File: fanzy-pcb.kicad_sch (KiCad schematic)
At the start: 27 parts, among them J1 Conn_01x04_Pin, J2 Screw_Terminal_01x05, P1 USB_C_Plug_USB2.0, Q1 IRLZ44N, SW1 SW_Push, U1 STM32G030F6Px, U2 AMS1117-3.3, U3 CH340N, U4 YAAJ_DCDC_StepDown_LM2596

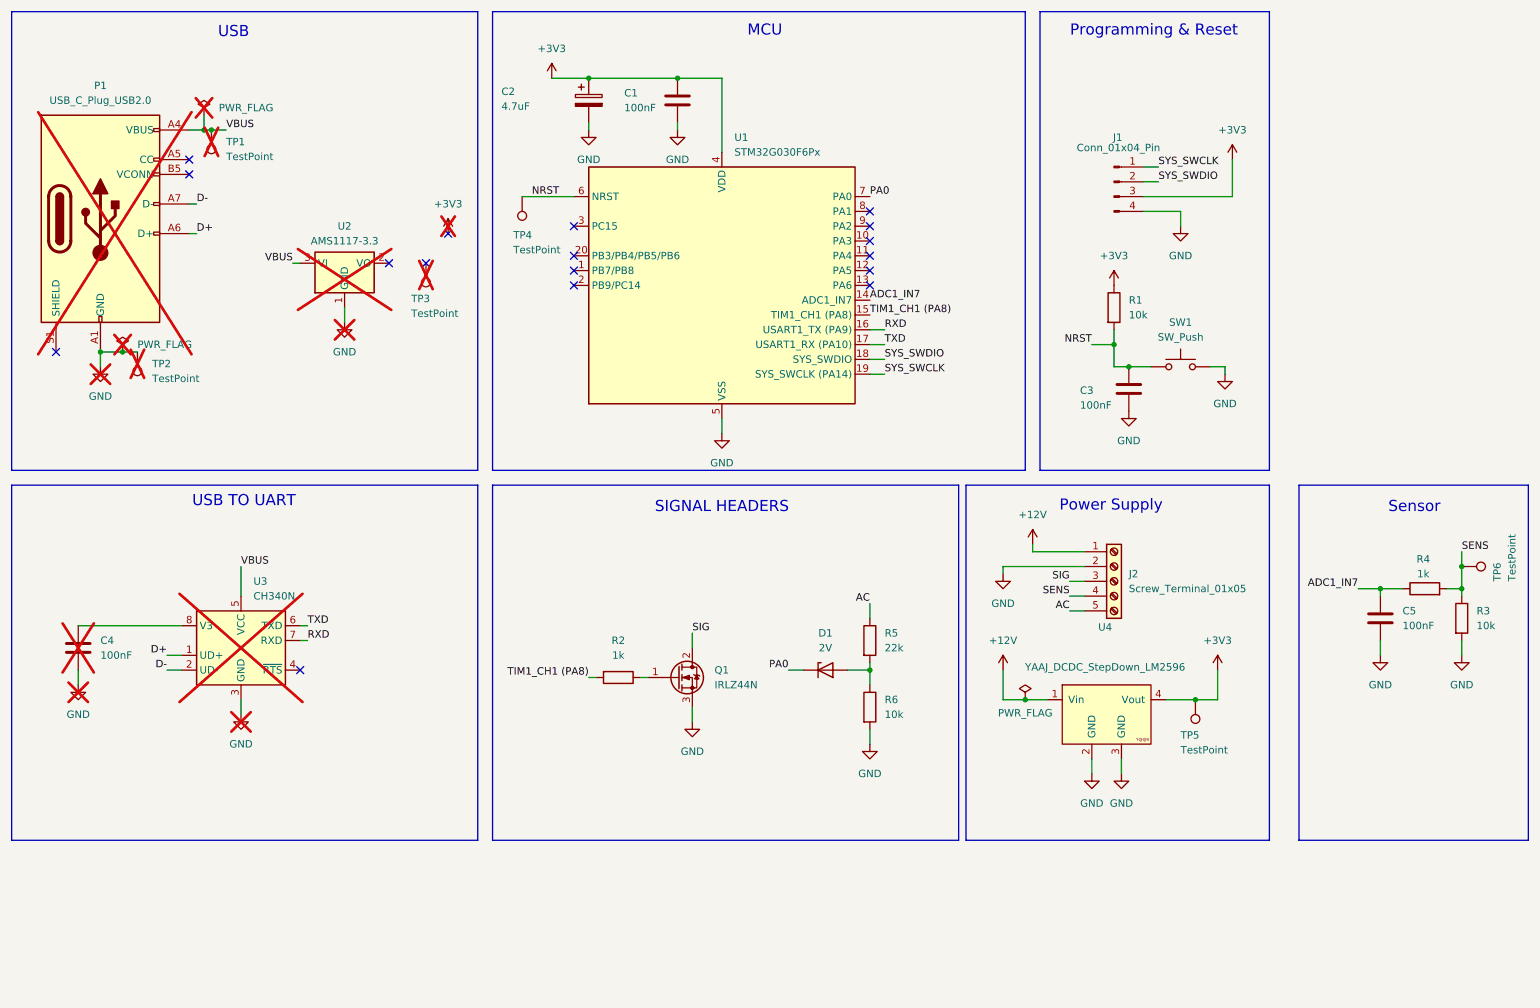
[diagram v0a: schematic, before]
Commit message: feat: uart port + rework
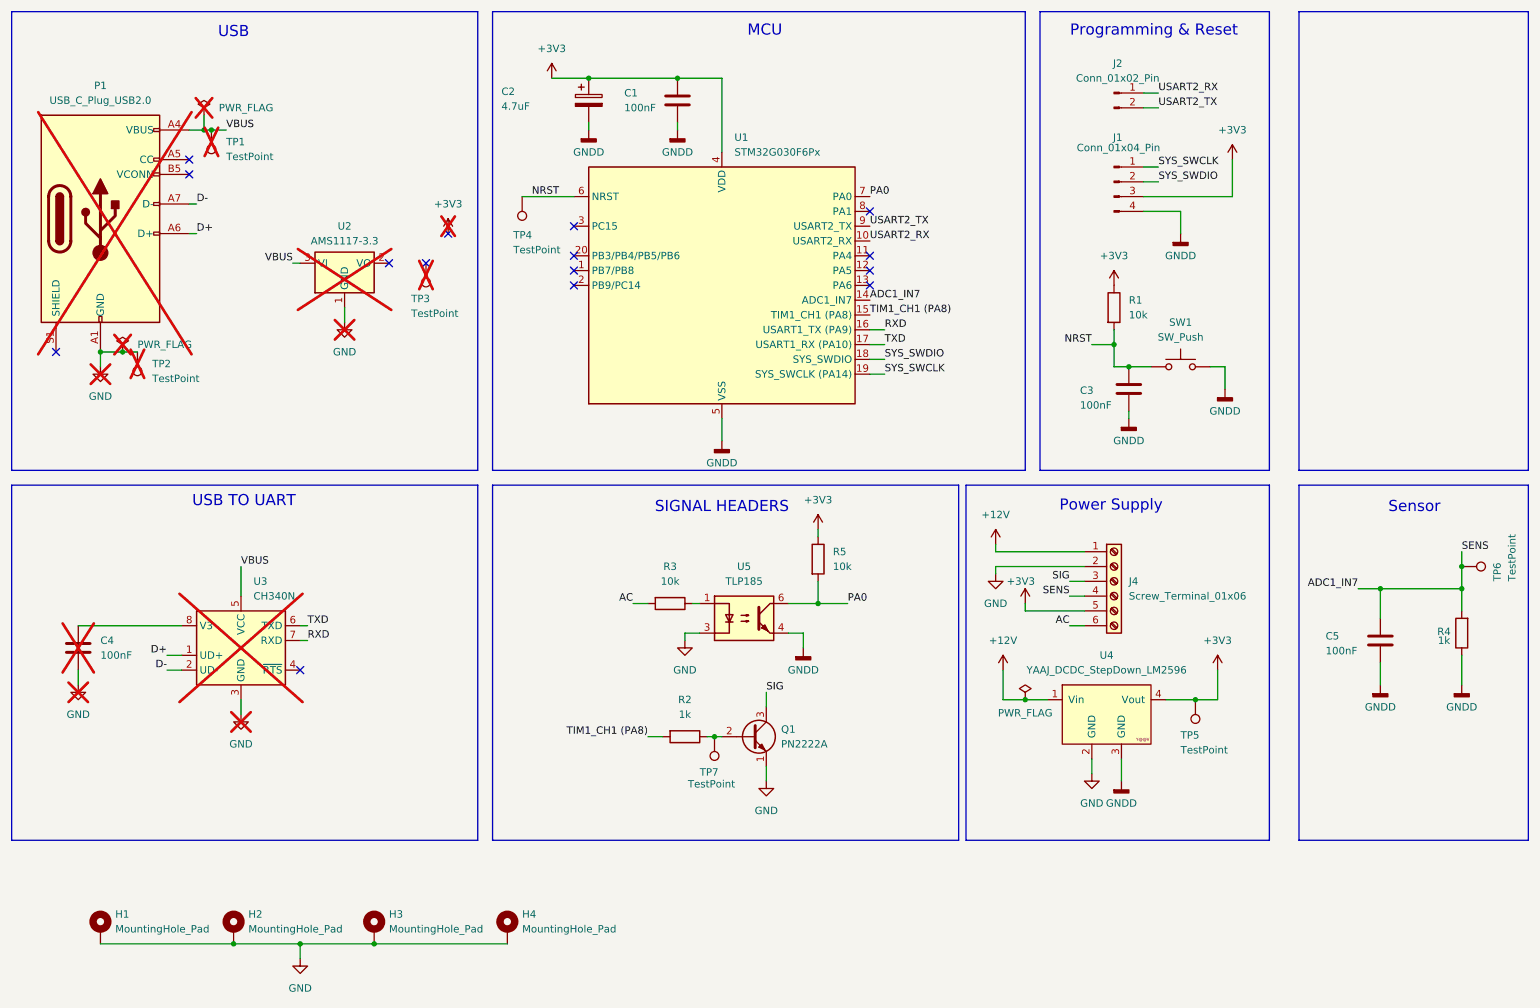
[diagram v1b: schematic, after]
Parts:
- removed D1: 2V, Diode_SMD:D_MiniMELF_Handsoldering, symbol Device:D_Zener
- removed J2: Screw_Terminal_01x05, TerminalBlock_Phoenix:TerminalBlock_Phoenix_MKDS-1,5-5-5.08_1x05_P5.08mm_Horizontal, symbol Connector:Screw_Terminal_01x05
- removed Q1: IRLZ44N, Package_TO_SOT_THT:TO-220-3_Vertical, symbol Transistor_FET:IRLZ44N
- removed R6: 10k, Resistor_SMD:R_0805_2012Metric_Pad1.20x1.40mm_HandSolder, symbol Device:R
- added H1, H2, H3, H4: MountingHole_Pad, MountingHole:MountingHole_3.2mm_M3_Pad_Via, symbol Mechanical:MountingHole_Pad
- added J2: Conn_01x02_Pin, Connector_PinHeader_2.54mm:PinHeader_1x02_P2.54mm_Vertical, symbol Connector:Conn_01x02_Pin
- added J4: Screw_Terminal_01x06, TerminalBlock_Phoenix:TerminalBlock_Phoenix_MKDS-1,5-6-5.08_1x06_P5.08mm_Horizontal, symbol Connector:Screw_Terminal_01x06
- added Q1: PN2222A, Package_TO_SOT_THT:TO-92_Inline, symbol Transistor_BJT:PN2222A
- added TP7: TestPoint, TestPoint:TestPoint_Pad_1.0x1.0mm, symbol Connector:TestPoint
- added U5: TLP185, Octocoupler:TLP185, symbol Isolator:TLP185
- R5: value 22k -> 10k
- SW1: footprint Button_Switch_SMD:SW_SPST_TL3342 -> Button_Switch_THT:SW_PUSH_6mm
- U4: footprint YAAJ:YAAJ_DCDC_StepDown_LM2596 -> DC-DC-Converters:YAAJ_DCDC_StepDown_LM2596
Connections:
- net +12V: now also J4.1 (Pin_1)
- net +3V3: now also R5.1, J4.5 (Pin_5)
- net AC: now also R3.2, J4.6 (Pin_6); no longer R5.1
- net ADC1_IN7: now also R4.2, TP6.1, J4.4 (Pin_4); no longer R4.1
- net GND: now also H1.1, H2.1, H3.1, H4.1, J4.2 (Pin_2), Q1.1 (E), U5.3; no longer C1.2, C2.2, C3.2, C5.2, J1.4 (Pin_4), R3.2, SW1.2, U1.5 (VSS), U4.3 (GND)
- net PA0: now also R5.2, U5.6
- net SIG: now also J4.3 (Pin_3), Q1.3 (C)
- net at R2.1: now also Q1.2 (B), TP7.1
- net USART2_RX: now reaches U1.10 (PA3)
- net USART2_RX: now also J2.1 (Pin_1)
- net USART2_TX: now reaches U1.9 (PA2)
- net USART2_TX: now also J2.2 (Pin_2)
- removed net SENS: R3.1, R4.2, TP6.1
- new net: R3.1, U5.1
- new net GNDD: C1.2, C2.2, C3.2, C5.2, J1.4 (Pin_4), R4.1, SW1.2, U1.5 (VSS), U4.3 (GND), U5.4
- no-connect marks 17 -> 15
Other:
- moved on the sheet: C5, R2, R4

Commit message: rework: switching to the STM32G031J6M6 series
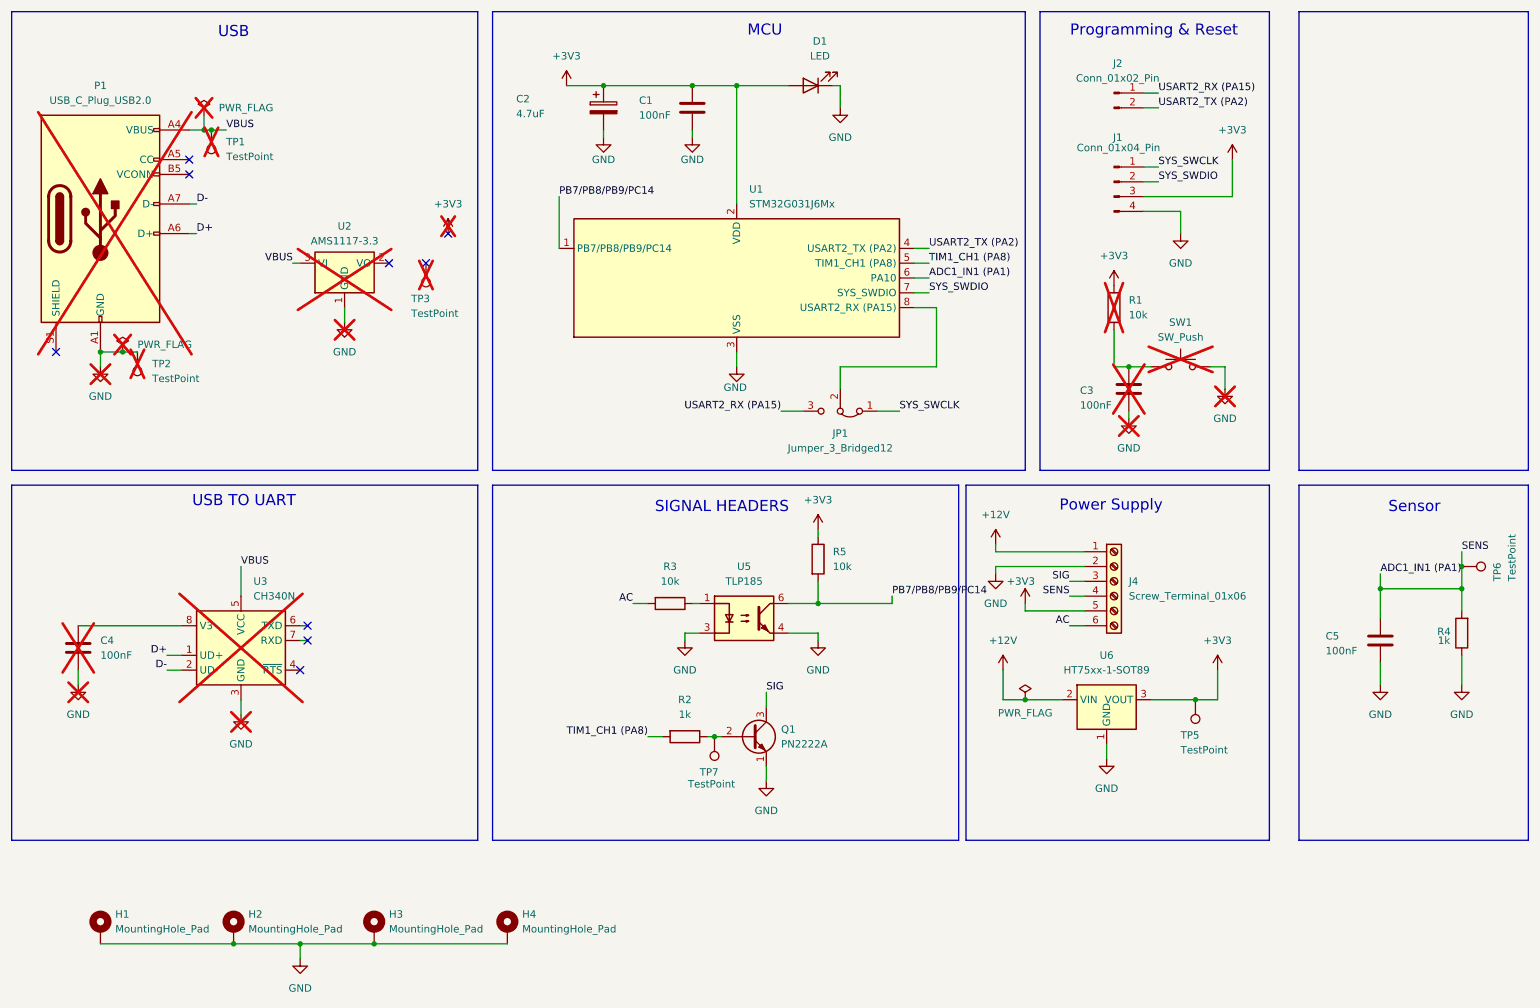
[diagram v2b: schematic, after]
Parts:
- removed TP4: TestPoint, TestPoint:TestPoint_Pad_1.0x1.0mm, symbol Connector:TestPoint
- removed U1: STM32G030F6Px, Package_SO:TSSOP-20_4.4x6.5mm_P0.65mm, symbol MCU_ST_STM32G0:STM32G030F6Px
- removed U4: YAAJ_DCDC_StepDown_LM2596, DC-DC-Converters:YAAJ_DCDC_StepDown_LM2596, symbol YAAJ:YAAJ_DCDC_StepDown_LM2596
- added D1: LED, LED_SMD:LED_0805_2012Metric_Pad1.15x1.40mm_HandSolder, symbol Device:LED
- added JP1: Jumper_3_Bridged12, Connector_PinHeader_2.54mm:PinHeader_1x03_P2.54mm_Vertical, symbol Jumper:Jumper_3_Bridged12
- added U1: STM32G031J6Mx, Package_SO:SOIC-8_3.9x4.9mm_P1.27mm, symbol MCU_ST_STM32G0:STM32G031J6Mx
- added U6: HT75xx-1-SOT89, Package_TO_SOT_SMD:SOT-89-3_Handsoldering, symbol Regulator_Linear:HT75xx-1-SOT89
- C3, R1, SW1: now not fitted; now left out of the parts list
- C4, P1, TP1, TP2, TP3, U2, U3: now left out of the parts list
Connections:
- net GNDD is gone; now on net GND: C1.2, C2.2, C3.2, C5.2, J1.4 (Pin_4), R4.1, SW1.2, U5.4
- net +12V: now also U6.2 (VIN)
- net +3V3: now also D1.2 (A), U1.2 (VDD), U6.3 (VOUT)
- net GND: now also D1.1 (K), U1.3 (VSS), U6.1 (GND)
- net SYS_SWCLK: now also JP1.1 (A)
- net SYS_SWDIO: now also U1.7 (PA13)
- net TIM1_CH1 (PA8): now also U1.5 (PA8/PA9/PA11/PB0/PB1)
- net ADC1_IN7 renamed ADC1_IN1 (PA1)
- net ADC1_IN1 (PA1): now also U1.6 (PA10/PA12)
- net NRST: no longer names the net of C3.1, R1.2, SW1.1
- net PA0 renamed PB7/PB8/PB9/PC14
- net PB7/PB8/PB9/PC14: now also U1.1 (PB7/PB8/PB9/PC14)
- net RXD: no longer names the net of U3.7 (RXD)
- net TXD: no longer names the net of U3.6 (TXD)
- net USART2_RX renamed USART2_RX (PA15)
- net USART2_RX (PA15): now also JP1.3 (B)
- net USART2_TX renamed USART2_TX (PA2)
- net USART2_TX (PA2): now also U1.4 (PA0/PA1/PA2/PF2)
- new net: JP1.2 (C), U1.8 (PA14/PA15/PB5/PB6)
- no-connect marks 15 -> 9
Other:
- moved on the sheet: C1, C2

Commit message: incl: pcb
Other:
- title: (none) -> Fanzy - By Mahdi Husain
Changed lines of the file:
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@@
 	(generator_version "9.0")
 	(paper "A4")
+	(title_block
+		(title "Fanzy - By Mahdi Husain")
+		(date "2026-06-12")
+		(rev "V2.0")
+	)
 	(rectangle
 		(start 15.24 96.52)
